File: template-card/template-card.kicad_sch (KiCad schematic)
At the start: 3 parts, among them J1 Conn_01x10_Pin, SW1 SW_DPDT_x2

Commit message: blergh
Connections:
- net 24v: now also J2.7 (A); no longer J2.2 (B)
- net 5v: now also J2.9 (C); no longer J2.8 (B)
- net GND2: now also J2.2 (B), J2.8 (B); no longer J2.7 (A), J2.9 (C)
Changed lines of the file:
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@@
   (junction (at 186.69 124.46) (diameter 0) (color 0 0 0 0)
+  )
+  (junction (at 156.21 119.38) (diameter 0) (color 0 0 0 0)
   )
   (junction (at 201.93 124.46) (diameter 0) (color 0 0 0 0)
   )
+  (junction (at 123.19 119.38) (diameter 0) (color 0 0 0 0)
+  )
   (junction (at 194.31 124.46) (diameter 0) (color 0 0 0 0)
   )
-  (junction (at 151.13 119.38) (diameter 0) (color 0 0 0 0)
-  )
-  (junction (at 161.29 119.38) (diameter 0) (color 0 0 0 0)
-  )
-  (wire (pts (xy 156.21 115.57) (xy 156.21 121.92))
-    (stroke (width 0) (type default))
-  )
-  (wire (pts (xy 123.19 119.38) (xy 151.13 119.38))
+  (wire (pts (xy 118.11 119.38) (xy 123.19 119.38))
     (stroke (width 0) (type default))
   )
   (wire (pts (xy 180.975 68.58) (xy 180.975 74.93))
+    (stroke (width 0) (type default))
+  )
+  (wire (pts (xy 118.11 119.38) (xy 118.11 121.92))
     (stroke (width 0) (type default))
   )
@@
     (stroke (width 0) (type default))
   )
-  (wire (pts (xy 161.29 119.38) (xy 163.83 119.38))
+  (wire (pts (xy 123.19 119.38) (xy 156.21 119.38))
     (stroke (width 0) (type default))
   )
   (wire (pts (xy 199.39 119.38) (xy 199.39 127))
+    (stroke (width 0) (type default))
+  )
+  (wire (pts (xy 156.21 119.38) (xy 156.21 121.92))
+    (stroke (width 0) (type default))
+  )
+  (wire (pts (xy 151.13 115.57) (xy 151.13 121.92))
     (stroke (width 0) (type default))
   )
@@
   )
   (wire (pts (xy 184.15 114.3) (xy 184.15 127))
+    (stroke (width 0) (type default))
+  )
+  (wire (pts (xy 161.29 114.3) (xy 161.29 121.92))
     (stroke (width 0) (type default))
   )
@@
     (stroke (width 0) (type default))
   )
-  (wire (pts (xy 151.13 121.92) (xy 151.13 119.38))
-    (stroke (width 0) (type default))
-  )
   (wire (pts (xy 189.23 111.125) (xy 189.23 127))
     (stroke (width 0) (type default))
@@
     (stroke (width 0) (type default))
   )
-  (wire (pts (xy 151.13 119.38) (xy 161.29 119.38))
-    (stroke (width 0) (type default))
-  )
   (wire (pts (xy 113.03 115.57) (xy 113.03 121.92))
-    (stroke (width 0) (type default))
-  )
-  (wire (pts (xy 118.11 115.57) (xy 118.11 121.92))
     (stroke (width 0) (type default))
   )
@@
     (stroke (width 0) (type default))
   )
-  (wire (pts (xy 186.055 68.58) (xy 186.055 74.93))
+  (wire (pts (xy 156.21 119.38) (xy 163.83 119.38))
     (stroke (width 0) (type default))
   )
-  (wire (pts (xy 161.29 121.92) (xy 161.29 119.38))
+  (wire (pts (xy 186.055 68.58) (xy 186.055 74.93))
     (stroke (width 0) (type default))
   )
@@
   (wire (pts (xy 176.53 101.6) (xy 176.53 105.41))
     (stroke (width 0) (type default))
-  )
-  (label "24v" (at 118.11 115.57 0) (fields_autoplaced)
-    (effects (font (size 1.27 1.27)) (justify left bottom))
   )
   (label "scl" (at 186.055 68.58 0) (fields_autoplaced)
@@
   )
   (label "rx1{slash}scl1" (at 191.77 113.665 0) (fields_autoplaced)
+    (effects (font (size 1.27 1.27)) (justify left bottom))
+  )
+  (label "5v" (at 161.29 114.3 0) (fields_autoplaced)
     (effects (font (size 1.27 1.27)) (justify left bottom))
   )
@@
     (effects (font (size 1.27 1.27)) (justify left bottom))
   )
+  (label "24v" (at 151.13 115.57 0) (fields_autoplaced)
+    (effects (font (size 1.27 1.27)) (justify left bottom))
+  )
   (label "tx0{slash}sda0" (at 176.53 105.41 180) (fields_autoplaced)
     (effects (font (size 1.27 1.27)) (justify right bottom))
@@
     (effects (font (size 1.27 1.27)) (justify left bottom))
   )
-  (label "5v" (at 156.21 115.57 0) (fields_autoplaced)
-    (effects (font (size 1.27 1.27)) (justify left bottom))
-  )

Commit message: Updated Repo
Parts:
- J1: symbol Connector:Conn_01x10_Pin -> 2024-backplane:Backplane_Card_Edge
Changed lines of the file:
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@@
     )
   )
-  (symbol (lib_id "2024-backplane:MR60PW-M_X3") (at 121.92 121.92 0) (mirror x) (unit 1)
+  (symbol (lib_name "MR60PW-M_X3_1") (lib_id "2024-backplane:MR60PW-M_X3") (at 121.92 121.92 0) (mirror x) (unit 1)
     (in_bom yes) (on_board yes) (dnp no) (fields_autoplaced)
     (property "Reference" "J2" (at 125.73 128.27 0)
@@
     )
   )
-  (symbol (lib_id "Connector:Conn_01x10_Pin") (at 189.23 132.08 90) (unit 1)
+  (symbol (lib_id "2024-backplane:Backplane_Card_Edge") (at 189.23 129.54 0) (unit 1)
     (in_bom yes) (on_board yes) (dnp no) (fields_autoplaced)
-    (property "Reference" "J1" (at 190.5 134.62 90)
-      (effects (font (size 1.27 1.27)))
+    (property "Reference" "J1" (at 205.105 134.62 0)
+      (effects (font (size 1.27 1.27)) (justify left))
     )
-    (property "Value" "Conn_01x10_Pin" (at 190.5 137.16 90)
-      (effects (font (size 1.27 1.27)))
+    (property "Value" "Conn_01x10_Pin" (at 205.105 137.16 0)
+      (effects (font (size 1.27 1.27)) (justify left))
     )
-    (property "Footprint" "2024-backplane:CardEdge_2x10" (at 189.23 132.08 0)
+    (property "Footprint" "2024-backplane:CardEdge_2x10" (at 191.77 116.84 0)
       (effects (font (size 1.27 1.27)) hide)
     )
-    (property "Datasheet" "~" (at 189.23 132.08 0)
+    (property "Datasheet" "~" (at 191.77 116.84 0)
       (effects (font (size 1.27 1.27)) hide)
     )

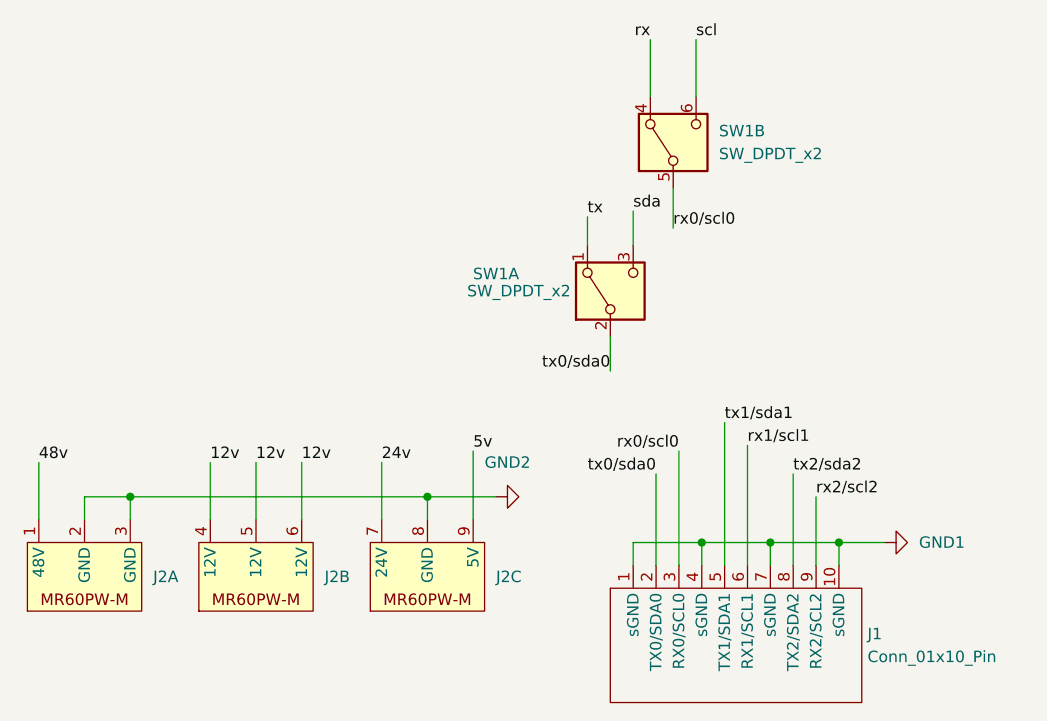
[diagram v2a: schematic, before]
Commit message: changed 12v lines to be seperate
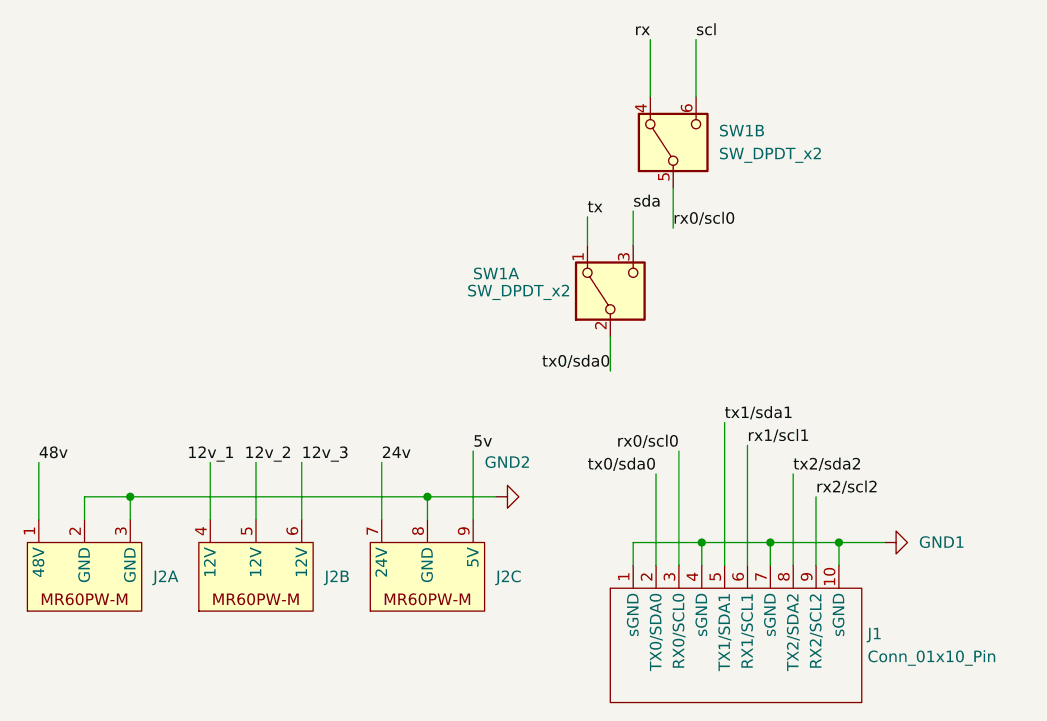
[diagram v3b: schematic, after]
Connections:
- removed net 12v: J2.4 (12V), J2.5 (12V), J2.6 (12V)
- new net 12v_3: J2.6 (12V)
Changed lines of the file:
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@@
     (effects (font (size 1.27 1.27)) (justify left bottom))
   )
-  (label "12v" (at 132.08 115.57 0) (fields_autoplaced)
+  (label "12v_1" (at 129.54 115.57 0) (fields_autoplaced)
     (effects (font (size 1.27 1.27)) (justify left bottom))
   )
@@
     (effects (font (size 1.27 1.27)) (justify left bottom))
   )
-  (label "12v" (at 142.24 115.57 0) (fields_autoplaced)
+  (label "12v_3" (at 142.24 115.57 0) (fields_autoplaced)
     (effects (font (size 1.27 1.27)) (justify left bottom))
   )
@@
     (effects (font (size 1.27 1.27)) (justify right bottom))
   )
-  (label "12v" (at 137.16 115.57 0) (fields_autoplaced)
+  (label "12v_2" (at 135.89 115.57 0) (fields_autoplaced)
     (effects (font (size 1.27 1.27)) (justify left bottom))
   )
